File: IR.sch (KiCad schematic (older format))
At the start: 5 parts, among them U65 74LS173, U66 74LS173, U68 74LS173, U69 74LS173, U70 74LS245

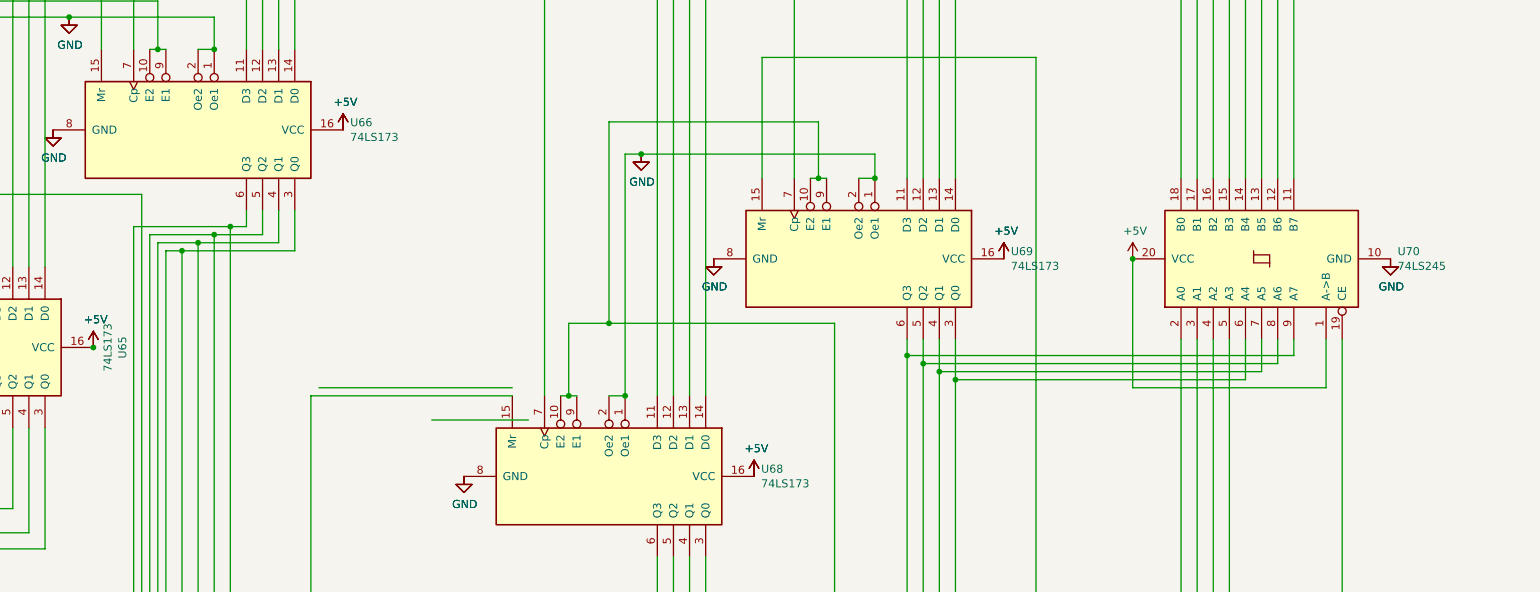
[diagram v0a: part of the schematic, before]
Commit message: using new RAM and ROM,15bits baby
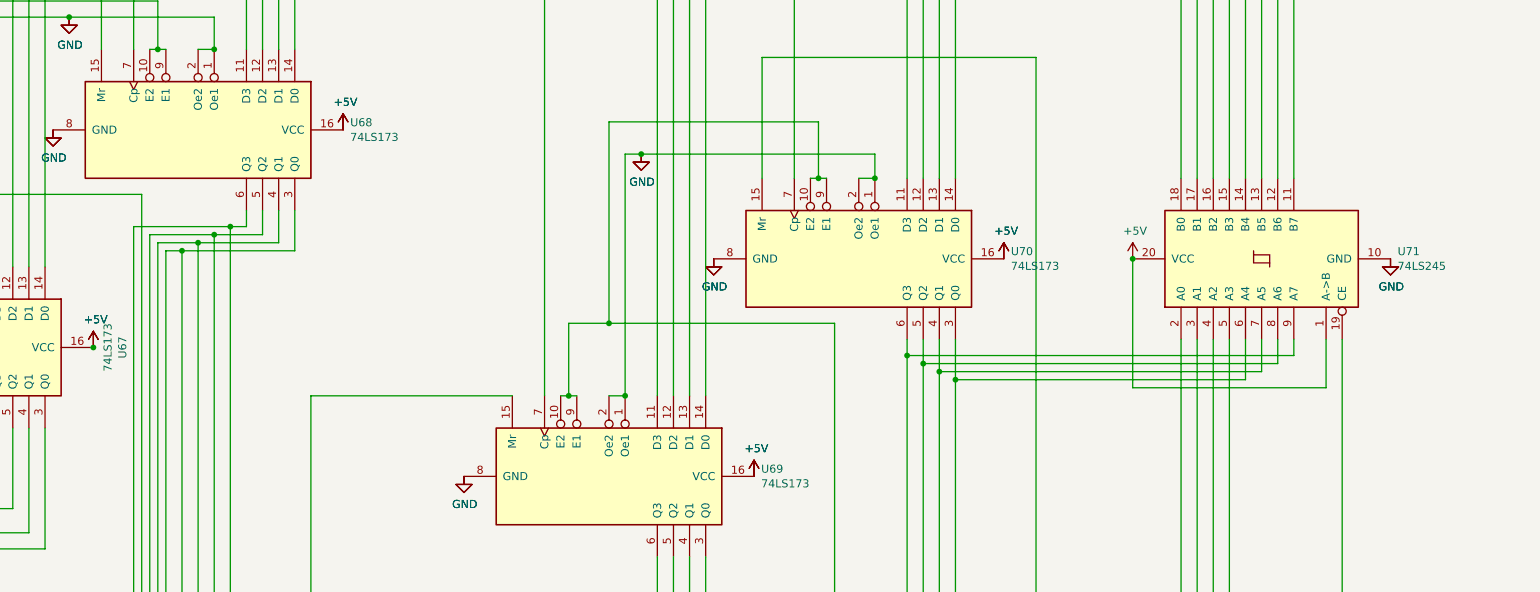
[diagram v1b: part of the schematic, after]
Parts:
- renumbered U65 to U67, U66 to U68, U68 to U69, U69 to U70, U70 to U71
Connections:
- wire segments 219 -> 217

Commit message: using new ROM in CU and more jumps
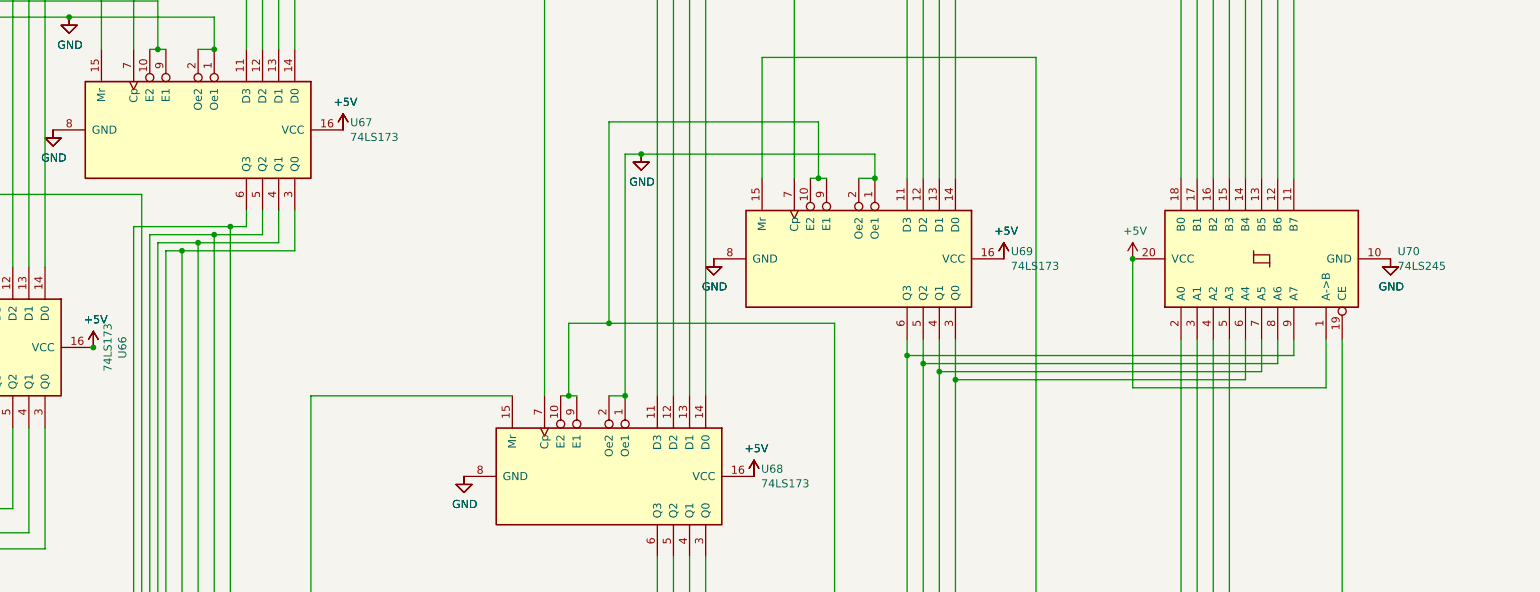
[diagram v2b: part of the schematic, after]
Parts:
- renumbered U67 to U66, U68 to U67, U69 to U68, U70 to U69, U71 to U70
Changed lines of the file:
@@
 AR Path="/603B766D/5F7C1E87" Ref="U?"  Part="1"
 AR Path="/5F74778C/5F7C1E87" Ref="U?"  Part="1"
-AR Path="/5F79B702/5F7C1E87" Ref="U67"  Part="1"
-F 0 "U67" H 4150 6331 50  0000 C CNN
+AR Path="/5F79B702/5F7C1E87" Ref="U66"  Part="1"
+F 0 "U66" H 4150 6331 50  0000 C CNN
 F 1 "74LS173" H 4150 6240 50  0000 C CNN
 F 2 "Package_DIP:DIP-16_W7.62mm" H 4150 5250 50  0001 C CNN
@@
 AR Path="/603B766D/5F7C1F08" Ref="U?"  Part="1"
 AR Path="/5F74778C/5F7C1F08" Ref="U?"  Part="1"
-AR Path="/5F79B702/5F7C1F08" Ref="U68"  Part="1"
-F 0 "U68" V 5654 4844 50  0000 L CNN
+AR Path="/5F79B702/5F7C1F08" Ref="U67"  Part="1"
+F 0 "U67" V 5654 4844 50  0000 L CNN
 F 1 "74LS173" V 5745 4844 50  0000 L CNN
 F 2 "Package_DIP:DIP-16_W7.62mm" H 5700 3900 50  0001 C CNN
@@
 AR Path="/603B766D/600A75A7" Ref="U?"  Part="1"
 AR Path="/5F74778C/600A75A7" Ref="U?"  Part="1"
-AR Path="/5F79B702/600A75A7" Ref="U71"  Part="1"
-F 0 "U71" V 12346 3856 50  0000 R CNN
+AR Path="/5F79B702/600A75A7" Ref="U70"  Part="1"
+F 0 "U70" V 12346 3856 50  0000 R CNN
 F 1 "74LS245" V 12255 3856 50  0000 R CNN
 F 2 "Package_DIP:DIP-20_W7.62mm" H 12300 4700 50  0001 C CNN
@@
 AR Path="/603B766D/5F7C1E93" Ref="U?"  Part="1"
 AR Path="/5F74778C/5F7C1E93" Ref="U?"  Part="1"
-AR Path="/5F79B702/5F7C1E93" Ref="U70"  Part="1"
-F 0 "U70" V 9754 5644 50  0000 L CNN
+AR Path="/5F79B702/5F7C1E93" Ref="U69"  Part="1"
+F 0 "U69" V 9754 5644 50  0000 L CNN
 F 1 "74LS173" V 9845 5644 50  0000 L CNN
 F 2 "Package_DIP:DIP-16_W7.62mm" H 9800 4700 50  0001 C CNN
@@
 AR Path="/603B766D/5F7C1F02" Ref="U?"  Part="1"
 AR Path="/5F74778C/5F7C1F02" Ref="U?"  Part="1"
-AR Path="/5F79B702/5F7C1F02" Ref="U69"  Part="1"
-F 0 "U69" V 8204 6994 50  0000 L CNN
+AR Path="/5F79B702/5F7C1F02" Ref="U68"  Part="1"
+F 0 "U68" V 8204 6994 50  0000 L CNN
 F 1 "74LS173" V 8295 6994 50  0000 L CNN
 F 2 "Package_DIP:DIP-16_W7.62mm" H 8250 6050 50  0001 C CNN

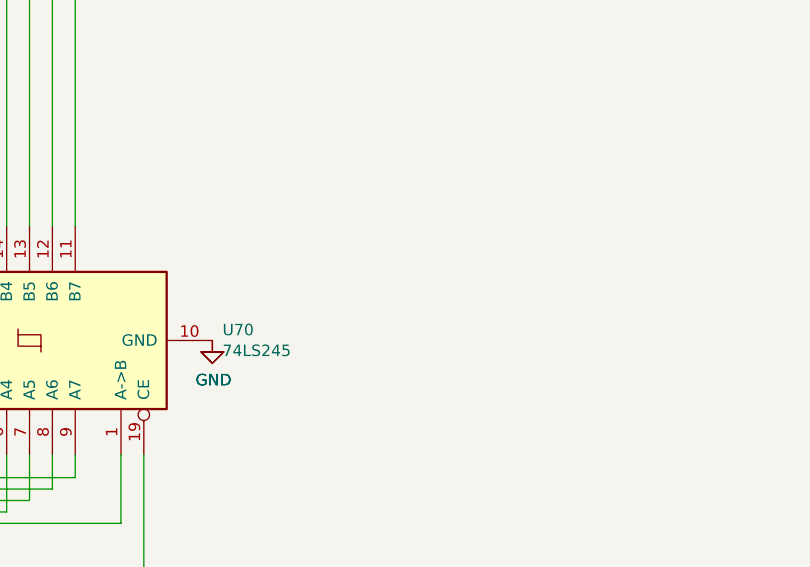
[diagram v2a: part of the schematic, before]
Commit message: added power caps
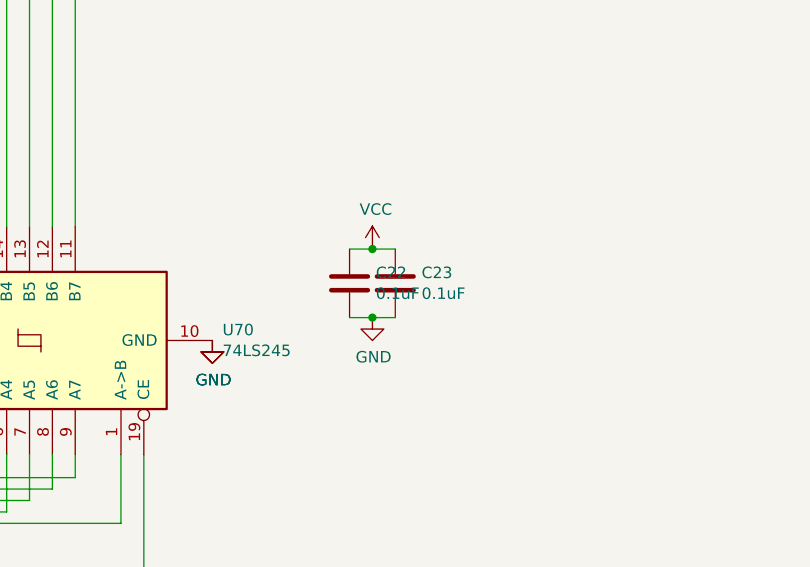
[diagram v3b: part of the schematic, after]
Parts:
- added C22, C23: 0.1uF, Capacitor_THT:CP_Axial_L10.0mm_D4.5mm_P15.00mm_Horizontal, symbol Device:C
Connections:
- net labels added: VCC
- wire segments 217 -> 221
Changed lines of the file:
@@
 $Descr A3 16535 11693
 encoding utf-8
-Sheet 17 21
+Sheet 16 21
 Title ""
 Date ""
@@
 Wire Wire Line
 	1600 7900 10200 7900
+$Comp
+L 16bitCpu-rescue:VCC-power #PWR?
+U 1 1 5FC9F24C
+P 13800 4300
+AR Path="/5FC9F24C" Ref="#PWR?"  Part="1"
+AR Path="/5F79B702/5FC9F24C" Ref="#PWR0275"  Part="1"
+F 0 "#PWR0275" H 13800 4150 50  0001 C CNN
+F 1 "VCC" H 13815 4473 50  0000 C CNN
+F 2 "" H 13800 4300 50  0001 C CNN
+F 3 "" H 13800 4300 50  0001 C CNN
+	1    13800 4300
+	1    0    0    -1
+$EndComp
+$Comp
+L 16bitCpu-rescue:GND-power #PWR?
+U 1 1 5FC9F252
+P 13800 4600
+AR Path="/5FC9F252" Ref="#PWR?"  Part="1"
+AR Path="/5F75E433/5FC9F252" Ref="#PWR?"  Part="1"
+AR Path="/5F79B702/5FC9F252" Ref="#PWR0276"  Part="1"
+F 0 "#PWR0276" H 13800 4350 50  0001 C CNN
+F 1 "GND" H 13805 4427 50  0000 C CNN
+F 2 "" H 13800 4600 50  0001 C CNN
+F 3 "" H 13800 4600 50  0001 C CNN
+	1    13800 4600
+	1    0    0    -1
+$EndComp
+Wire Wire Line
+	13800 4300 13900 4300
+Wire Wire Line
+	13900 4600 13800 4600
+$Comp
+L Device:C C?
+U 1 1 5FC9F25A
+P 13700 4450
+AR Path="/5F75E433/5FC9F25A" Ref="C?"  Part="1"
+AR Path="/5F79B702/5FC9F25A" Ref="C22"  Part="1"
+F 0 "C22" H 13815 4496 50  0000 L CNN
+F 1 "0.1uF" H 13815 4405 50  0000 L CNN
+F 2 "Capacitor_THT:CP_Axial_L10.0mm_D4.5mm_P15.00mm_Horizontal" H 13738 4300 50  0001 C CNN
+F 3 "" H 13700 4450 50  0001 C CNN
+	1    13700 4450
+	1    0    0    -1
+$EndComp
+Wire Wire Line
+	13800 4300 13700 4300
+Connection ~ 13800 4300
+Wire Wire Line
+	13700 4600 13800 4600
+Connection ~ 13800 4600
+$Comp
+L Device:C C?
+U 1 1 5FC9F264
+P 13900 4450
+AR Path="/5F75E433/5FC9F264" Ref="C?"  Part="1"
+AR Path="/5F79B702/5FC9F264" Ref="C23"  Part="1"
+F 0 "C23" H 14015 4496 50  0000 L CNN
+F 1 "0.1uF" H 14015 4405 50  0000 L CNN
+F 2 "Capacitor_THT:CP_Axial_L10.0mm_D4.5mm_P15.00mm_Horizontal" H 13938 4300 50  0001 C CNN
+F 3 "" H 13900 4450 50  0001 C CNN
+	1    13900 4450
+	1    0    0    -1
+$EndComp
 $EndSCHEMATC

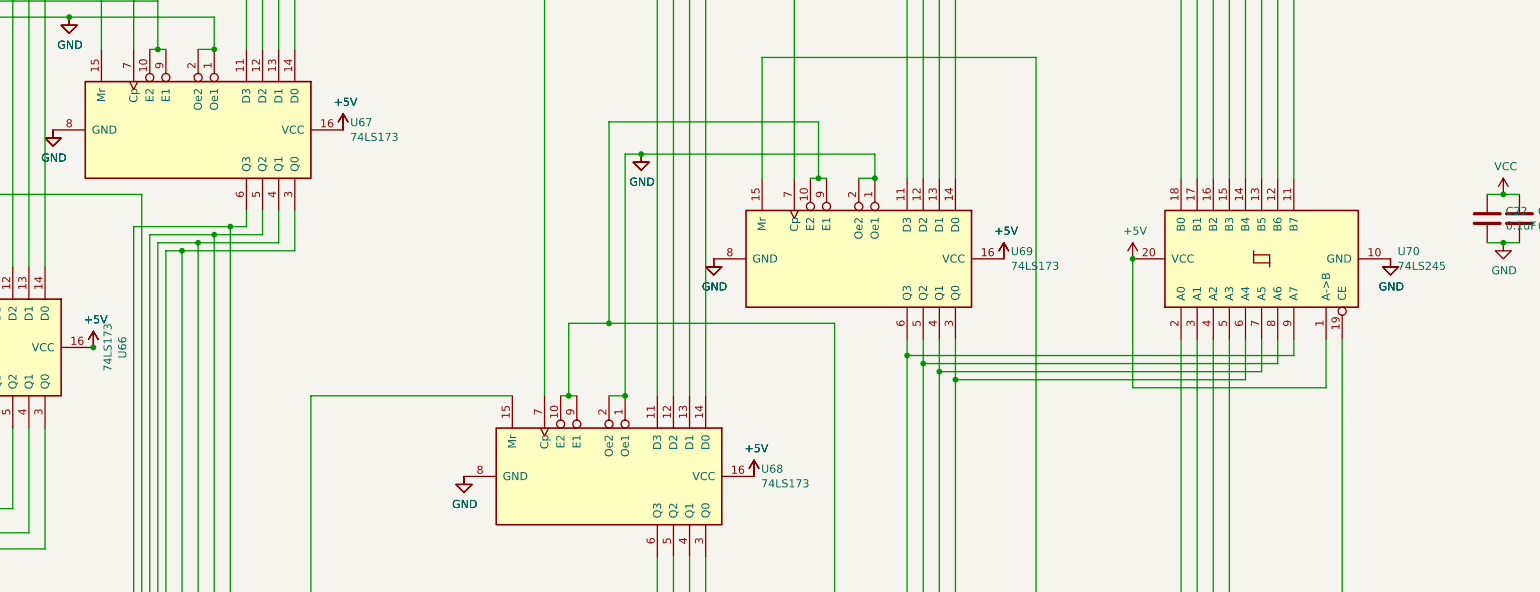
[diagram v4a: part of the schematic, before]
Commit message: added display
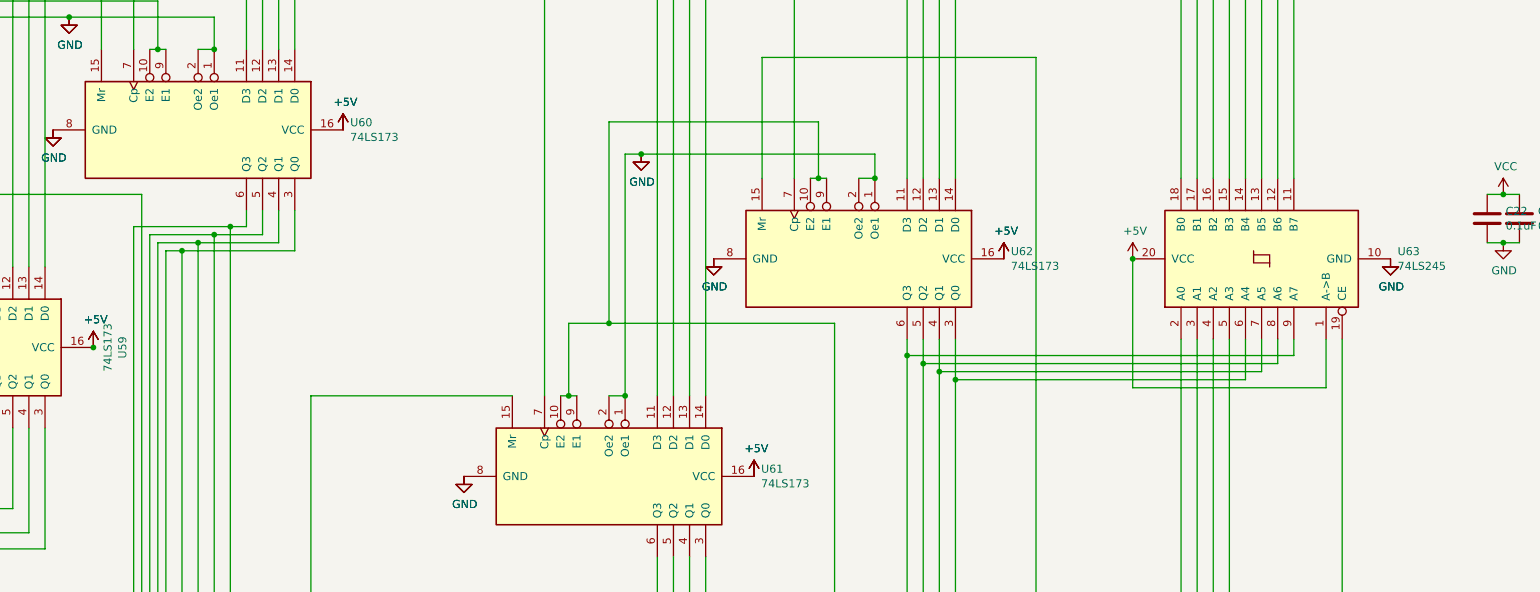
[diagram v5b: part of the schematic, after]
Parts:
- renumbered U66 to U59, U67 to U60, U68 to U61, U69 to U62, U70 to U63

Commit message: clean up
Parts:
- renumbered U59 to U61, U60 to U62, U61 to U63, U62 to U64, U63 to U65
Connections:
- wire segments 221 -> 204
